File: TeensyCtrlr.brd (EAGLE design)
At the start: 114.3 x 126.5 mm, 128 parts, among them IC1 LM358LM358, IC2 LM358LM358, IC3 LM358LM358, IC4 7805DT, Q1 2n3904, Q2 2n3904, Q3 2n3906

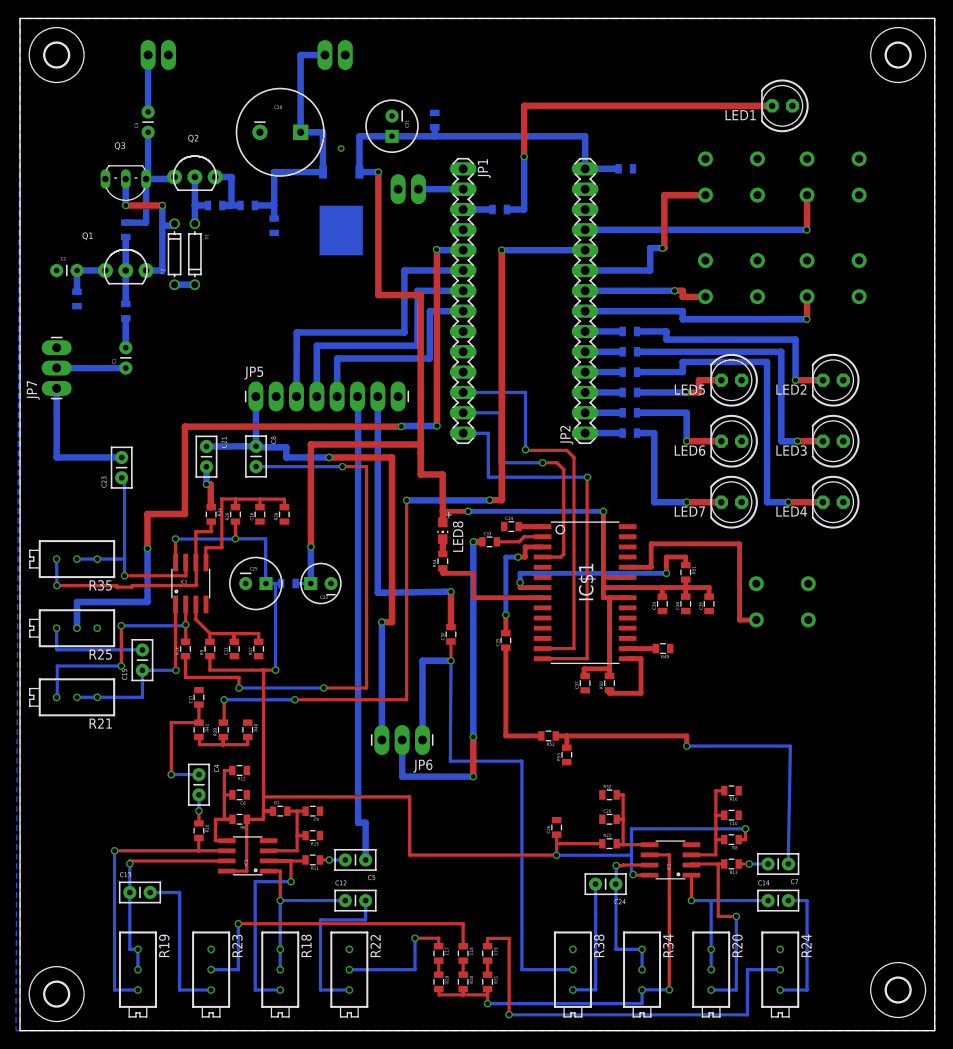
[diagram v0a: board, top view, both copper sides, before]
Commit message: 1.  Re-aligned lower right hole to match lower left 2.  Locked all holes, LED's and switches 3.  Added bit more clearance in DRC rules 4.  Reset trace widths to .024 5.  DRC rules checks passing except for some stop masks; need to smash few parts     and move silk screens.
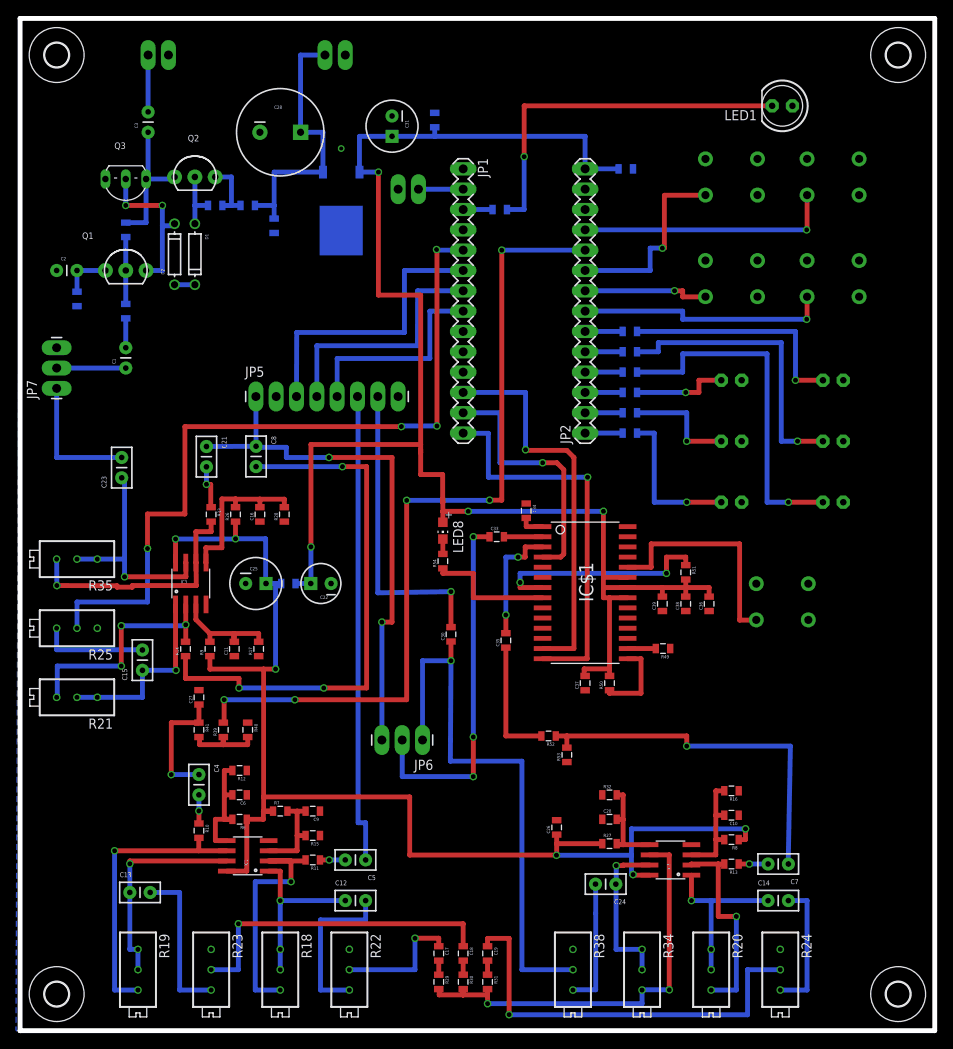
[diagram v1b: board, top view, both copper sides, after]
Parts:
- moved C34 2.71 mm to (63.2, 65.0), turned to 270 degrees
- moved C33 1.09 mm to (59.6, 61.7)
- moved U$3 0.51 mm to (109.7, 4.57)
- flipped LED2 to the bottom, turned to 0 degrees
- flipped LED3 to the bottom, turned to 0 degrees
- flipped LED4 to the bottom, turned to 0 degrees
- flipped LED5 to the bottom, turned to 0 degrees
- flipped LED6 to the bottom, turned to 0 degrees
- flipped LED7 to the bottom, turned to 0 degrees
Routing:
- net N$11: track 34.4 -> 36.7 mm
- net N$12: track 42.0 -> 44.1 mm
- net REC_AUDIO_IN: track 43.9 -> 45.5 mm
- net N$1: track 5.99 -> 4.83 mm

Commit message: 1.  Forgot to reverse LED 1, same position, re-locked it 2.  Fixed few trace alignments and un-routed grounds
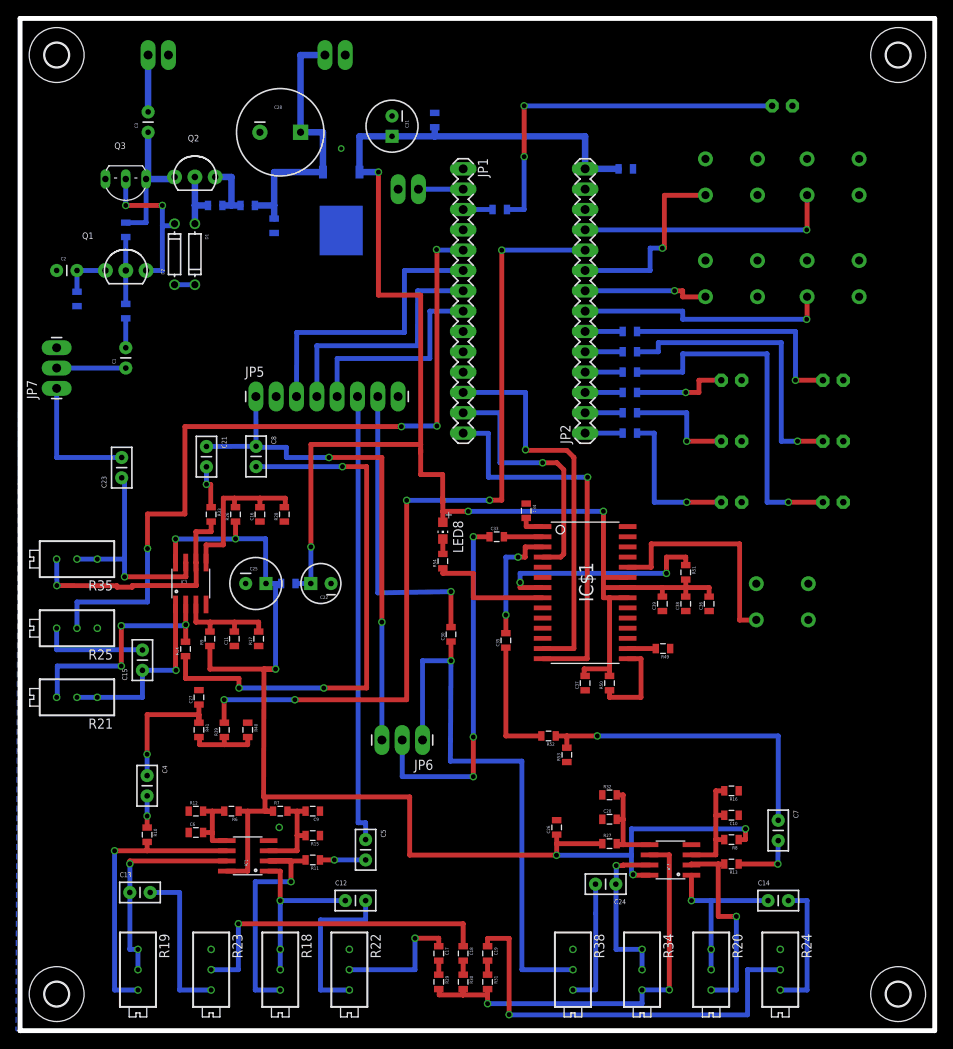
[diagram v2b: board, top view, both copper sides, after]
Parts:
- moved R12 7.46 mm to (22.0, 27.4), turned to 0 degrees
- moved C6 7.20 mm to (22.0, 24.8), turned to 0 degrees
- moved R10 6.50 mm to (15.9, 24.5)
- moved C4 6.48 mm to (15.9, 31.9)
- moved C7 5.61 mm to (94.7, 26.3), turned to 270 degrees
- moved C5 2.54 mm to (43.2, 23.9), turned to 270 degrees
- moved R6 1.44 mm to (26.4, 27.4)
- moved C11 1.27 mm to (26.8, 49.0)
- moved R17 1.27 mm to (29.8, 49.0)
- moved R9 1.27 mm to (23.7, 49.0)
- moved R39 0.13 mm to (25.5, 37.6)
- flipped LED1 to the bottom, turned to 0 degrees
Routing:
- net VOICEID_AUDIO: track 46.8 -> 39.8 mm
- net N$58: track 15.3 -> 9.29 mm
- net N$64: track 3.67 -> 7.81 mm
- net A5V: track 163.9 -> 167.7 mm
- net N$54: track 3.16 -> 5.70 mm
- net MIC_AUDIO_IN: track 58.9 -> 56.4 mm
- net RPTR_AUDIO_IN: track 67.4 -> 64.8 mm
- net CW_AUDIO: track 15.7 -> 17.4 mm
- net RESET: track 10.3 -> 11.3 mm
- net N$72: track 14.7 -> 13.7 mm
- net N$16: track 9.94 -> 9.11 mm
- net N$77: track 20.8 -> 21.6 mm
- net N$57: track 36.0 -> 35.4 mm
- net N$9: vias 1 -> 2

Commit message: Minor layout change (no holes/dimension changes) Generated Gerber files for test run at Seeed Studio Generated some .ps files Top and Bot layers for in house board generation
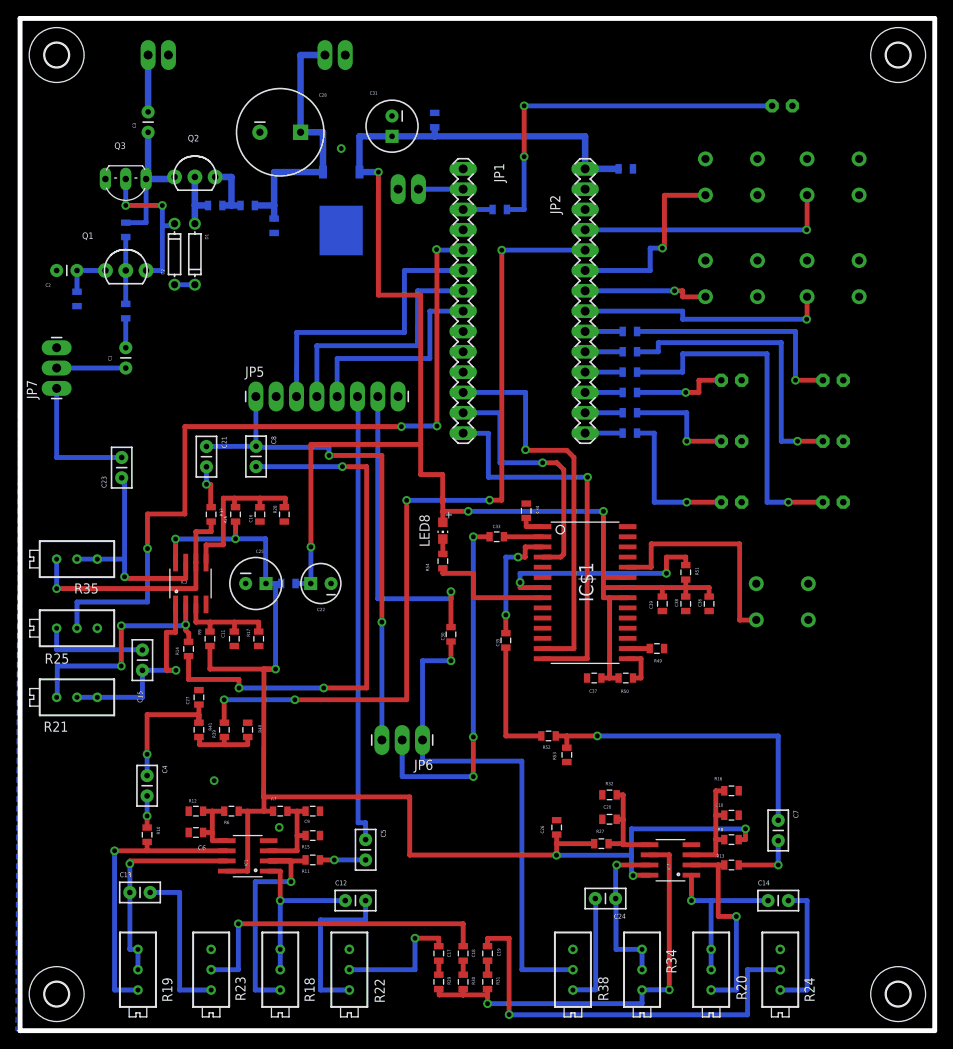
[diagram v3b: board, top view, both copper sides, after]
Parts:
- moved R50 2.13 mm to (75.7, 44.1), turned to 180 degrees
- moved C24 1.80 mm to (74.4, 16.5)
- moved C37 1.31 mm to (71.8, 44.1), turned to 0 degrees
- moved R27 1.02 mm to (72.6, 23.4)
- moved R49 0.76 mm to (79.6, 47.8)
- moved R14 0.38 mm to (21.1, 47.7)
- moved R13 0.13 mm to (88.9, 20.7)
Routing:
- net RPTR_MIC: track 69.8 -> 63.4 mm
- net RESET: track 11.3 -> 5.09 mm
- net N$74: track 24.0 -> 26.4 mm
- net VDD_5V: track 198.7 -> 196.5 mm
- net A5V: track 167.7 -> 165.8 mm
- net N$17: track 38.1 -> 39.7 mm
- net N$70: track 16.1 -> 14.6 mm
- net N$68: track 12.1 -> 13.0 mm
- net N$5: track 3.51 -> 2.75 mm
